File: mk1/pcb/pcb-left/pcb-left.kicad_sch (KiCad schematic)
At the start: 39 parts, among them J3 BAT, U1 xiao-ble

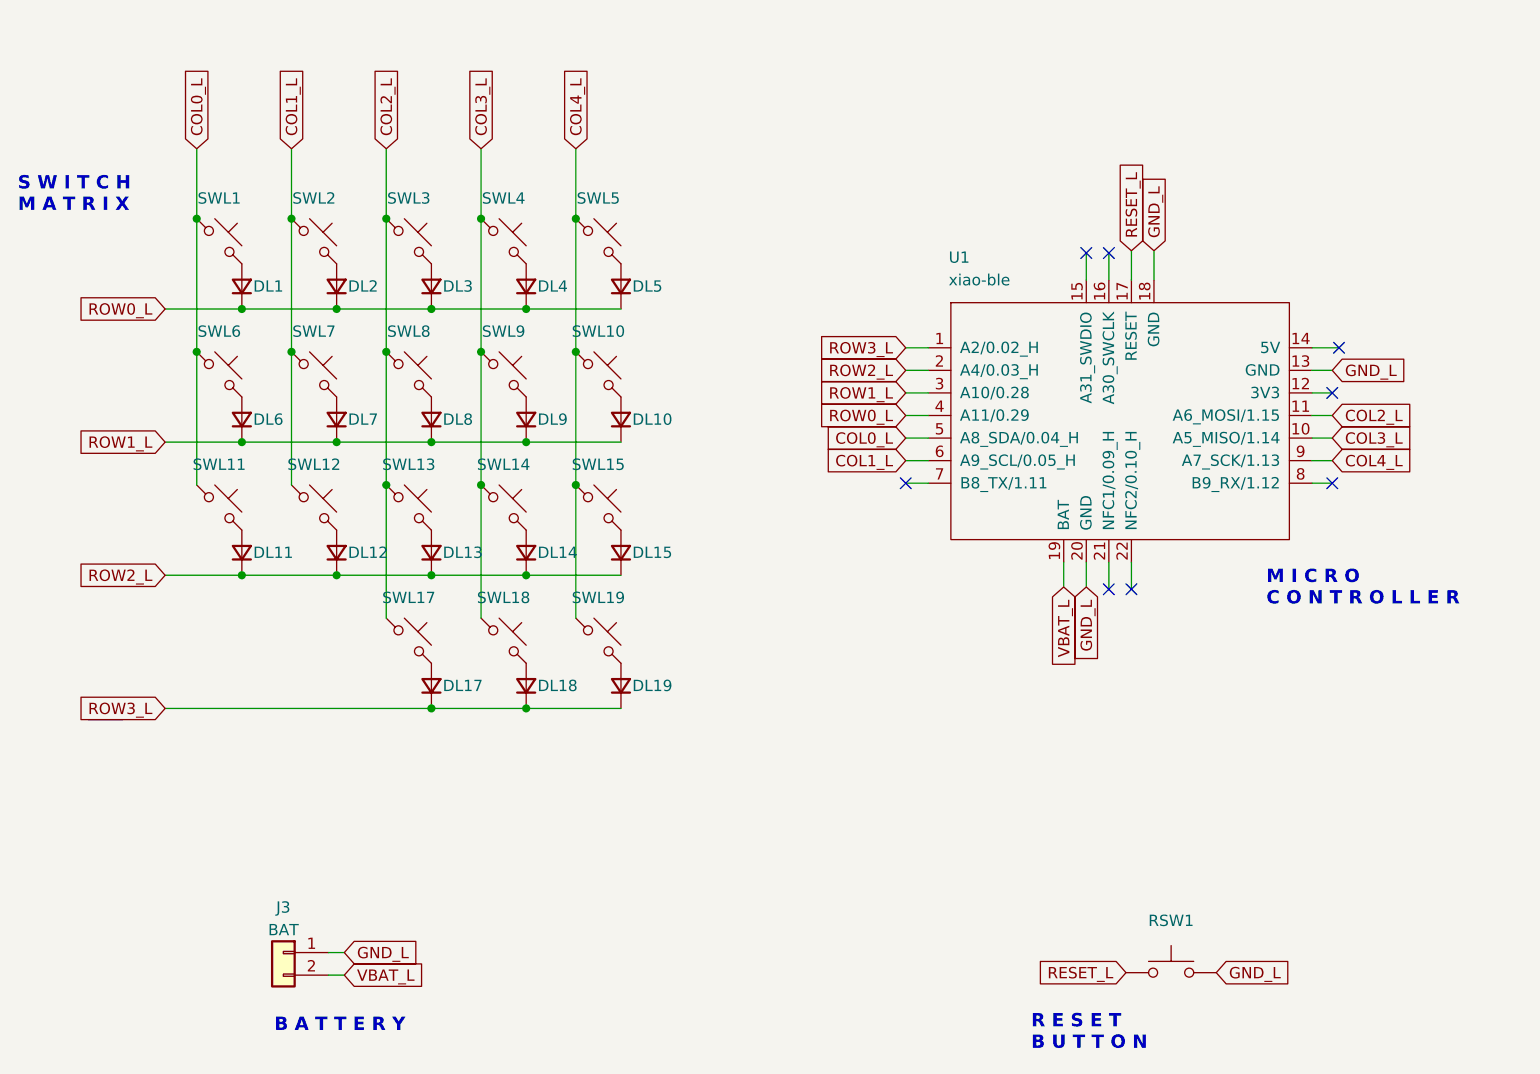
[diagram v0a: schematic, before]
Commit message: mk1/pcb-left: add power switch and debug header, update reset button
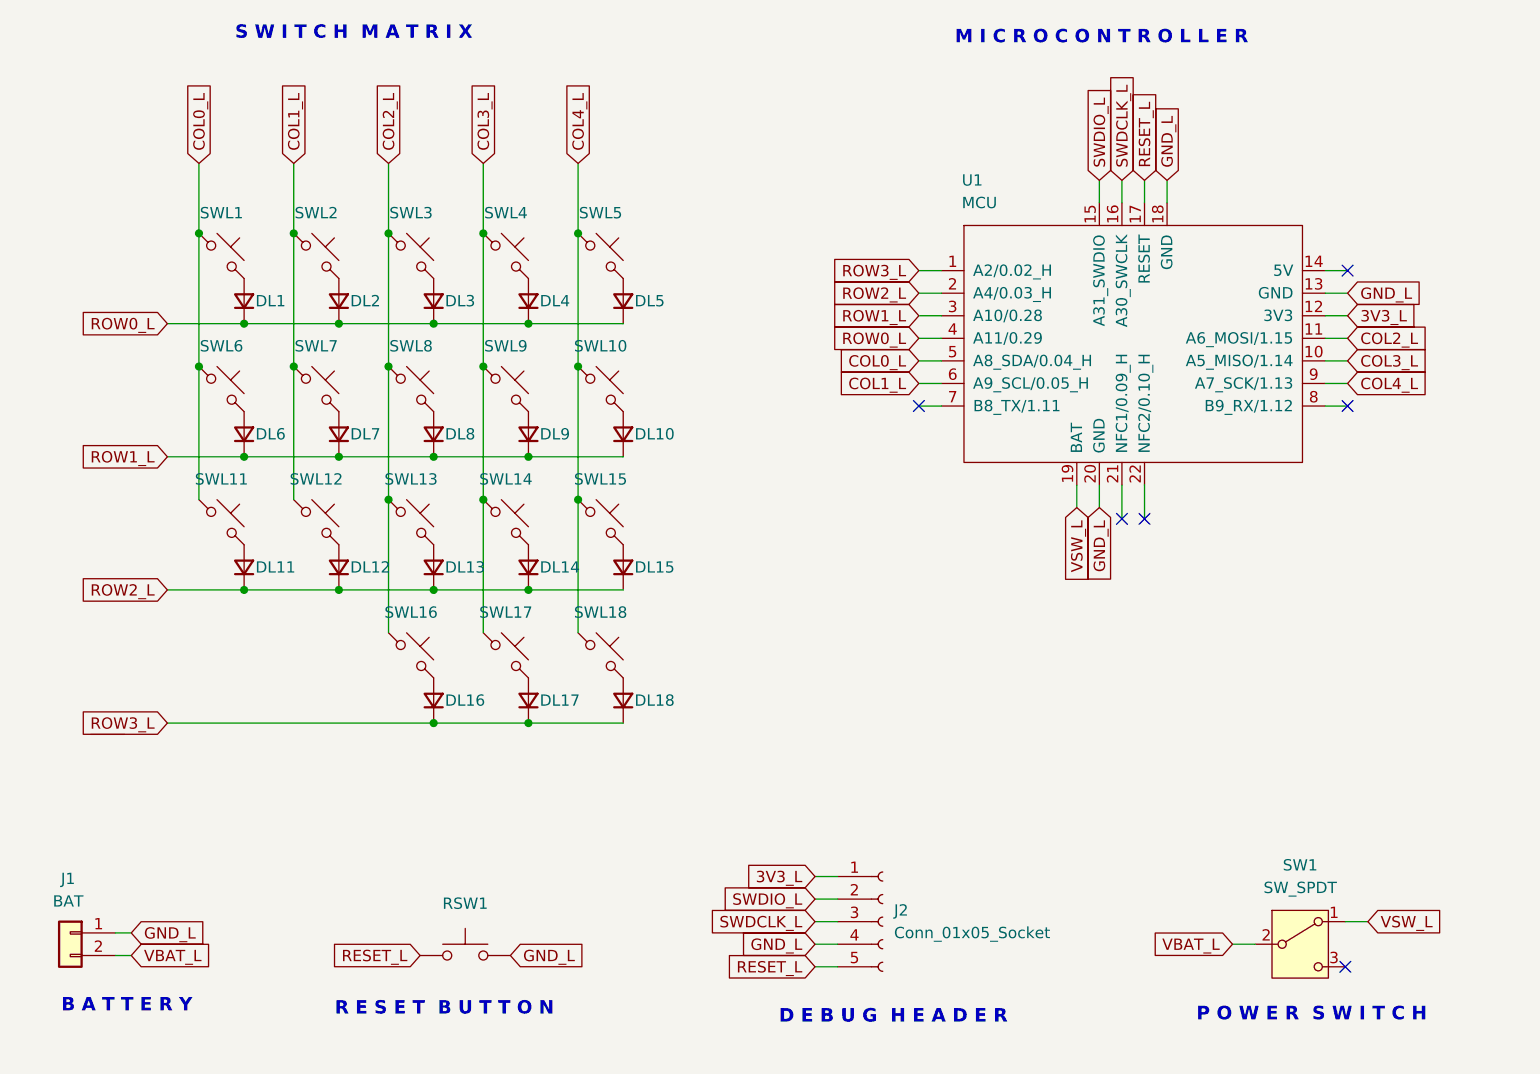
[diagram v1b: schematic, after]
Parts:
- added J2: Conn_01x05_Socket, Connector_PinHeader_2.54mm:PinHeader_1x05_P2.54mm_Vertical, symbol Connector:Conn_01x05_Socket
- added SW1: SW_SPDT, Button_Switch_SMD:SW_SPDT_PCM12, symbol Switch:SW_SPDT
- RSW1: footprint karmalib:SKHLLCA010 -> Button_Switch_SMD:SW_Push_1P1T_NO_CK_KMR2
- U1: value xiao-ble -> MCU
- renumbered DL17 to DL16, DL18 to DL17, DL19 to DL18, J3 to J1, SWL17 to SWL16, SWL18 to SWL17, SWL19 to SWL18
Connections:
- net GND_L: now also J2.4 (Pin_4)
- net RESET_L: now also J2.5 (Pin_5)
- net VBAT_L: now also SW1.2 (B); no longer U1.19 (BAT)
- net 3V3_L: now reaches U1.12 (3V3)
- net 3V3_L: now also J2.1 (Pin_1)
- net SWDIO_L: now reaches U1.15 (A31_SWDIO)
- net SWDIO_L: now also J2.2 (Pin_2)
- net SWDCLK_L: now reaches U1.16 (A30_SWCLK)
- net SWDCLK_L: now also J2.3 (Pin_3)
- new net VSW_L: SW1.1 (A), U1.19 (BAT)
- no-connect marks 8 -> 6
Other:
- note added: "D E B U G H E A D E R"
- note added: "P O W E R S W I T C H"
- moved on the sheet: DL1, DL10, DL11, DL12, DL13, DL14, DL15, DL16, DL17, DL18, DL2, DL3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
